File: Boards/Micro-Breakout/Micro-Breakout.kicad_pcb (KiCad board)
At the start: 2 copper layers, 92.7 x 54.6 mm, 38 parts, among them J1 Conn_01x04, J10 Conn_01x17, J11 Conn_01x04, J12 Conn_01x04, J13 Conn_01x02, J14 Conn_01x04, J16 Conn_01x04, J17 Conn_01x04, J18 Conn_01x04, J2 Conn_01x04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

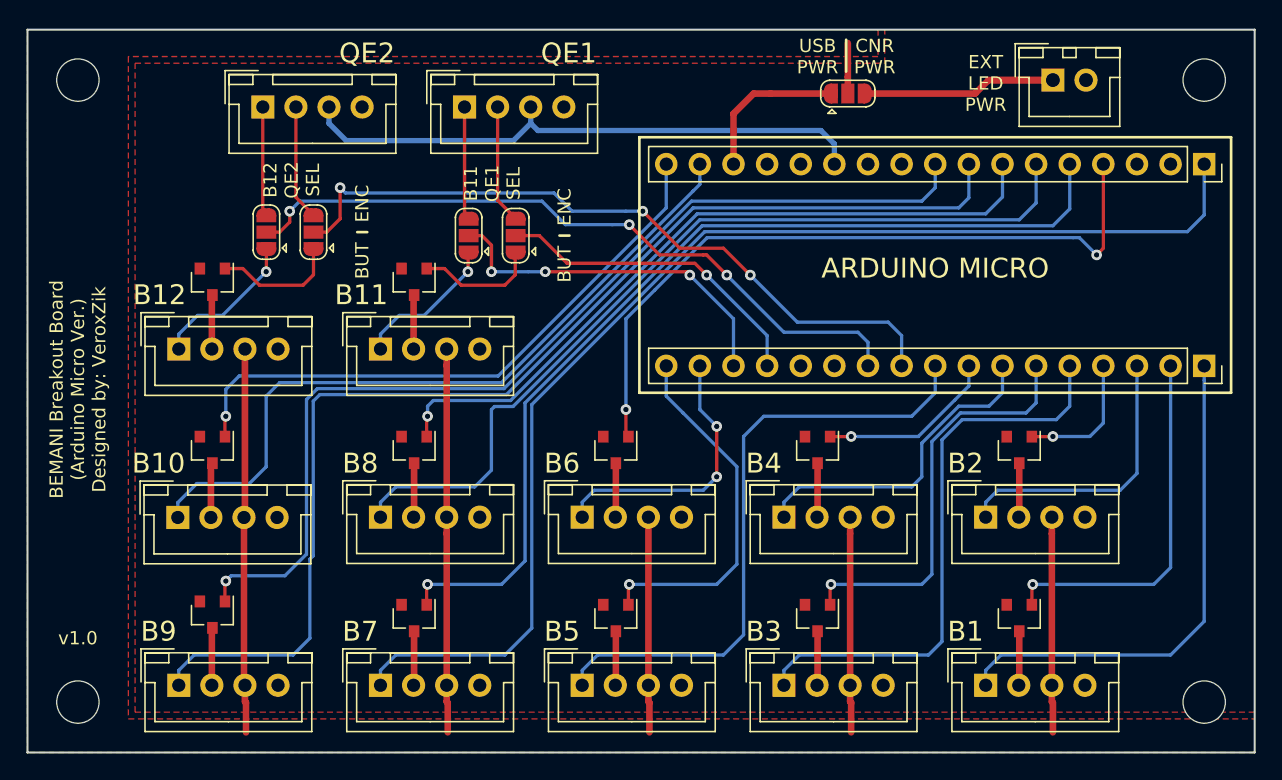
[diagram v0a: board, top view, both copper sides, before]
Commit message: Update both micro boards to v1.1
Fixes 5V on the LED connector
Adds pinout labels for Encoder / Button connectors
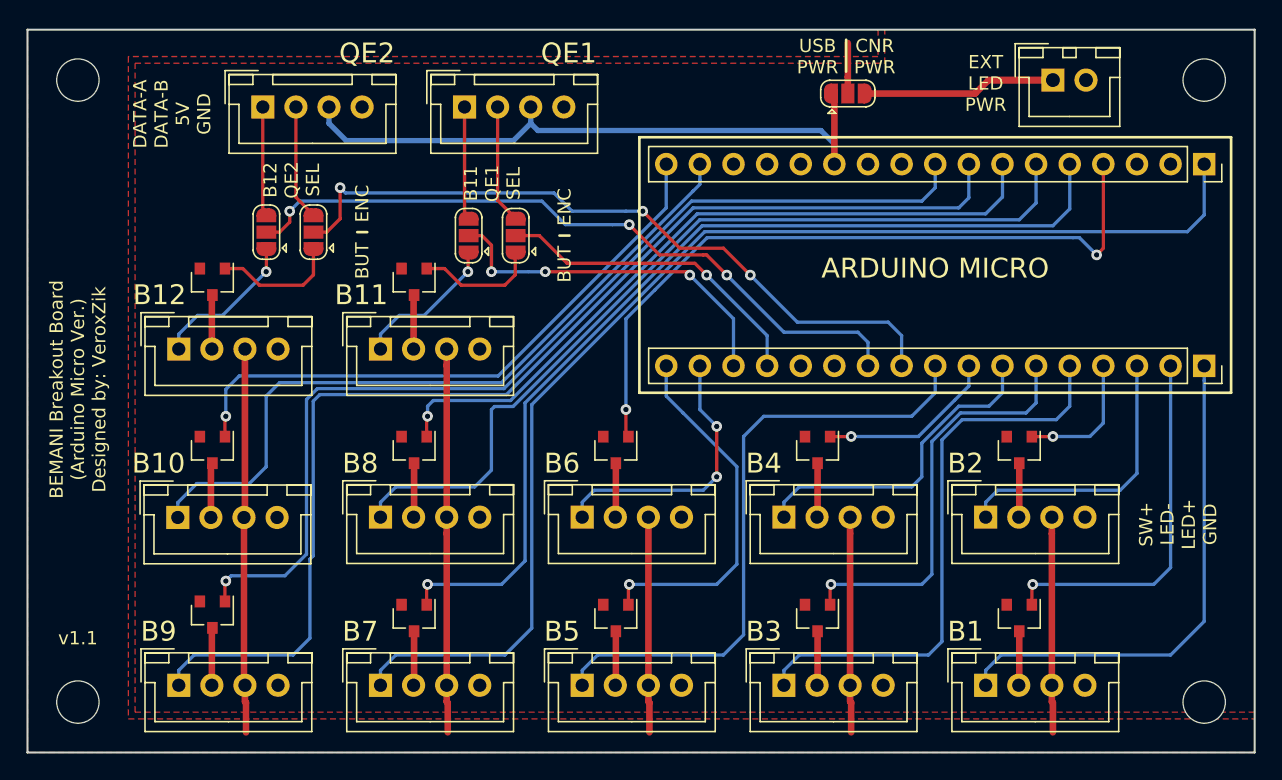
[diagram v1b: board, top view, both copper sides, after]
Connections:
- J7 pad 15: VBUS -> Net-(J7-Pad15)
- JP1 pad 1: VBUS -> +5V
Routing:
- net VBUS: track 11.8 -> 0.00 mm
- net +5V: track 43.9 -> 49.4 mm
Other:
- board text added: "DATA-A DATA-B 5V GND"
- board text added: "SW+ LED- LED+ GND"
- board text added: "v1.1"
- board text removed: "v1.0"

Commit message: Update Micro-Breakout board.
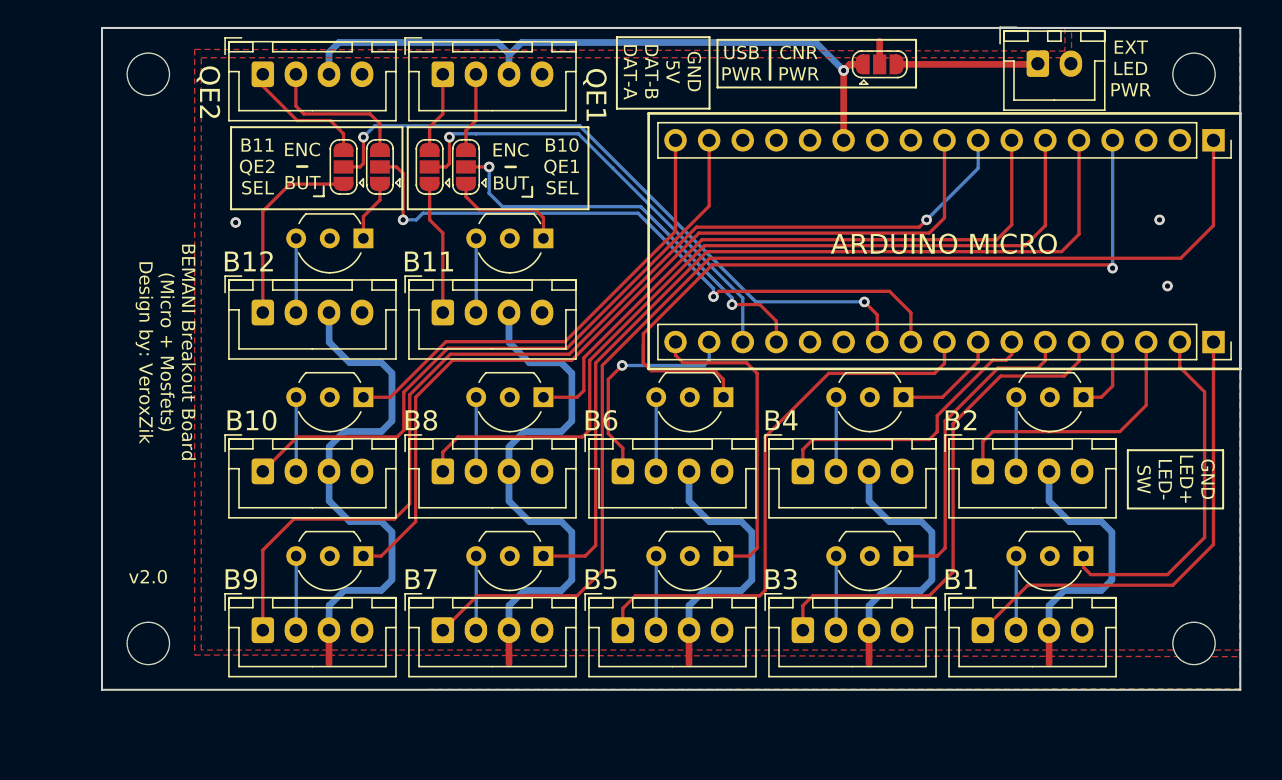
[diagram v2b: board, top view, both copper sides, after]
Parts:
- J1, J11, J12, J14, J16, J17, J18, J2, J3, J4, J5, J6, J8, J9: footprint Connectors_JST:JST_XH_B04B-XH-A_04x2.50mm_Straight -> Connector_JST:JST_XH_B4B-XH-A_1x04_P2.50mm_Vertical
- J13: footprint Connectors_JST:JST_XH_B02B-XH-A_02x2.50mm_Straight -> Connector_JST:JST_XH_B2B-XH-A_1x02_P2.50mm_Vertical
- Q1, Q10, Q11, Q12, Q2, Q3, Q4, Q5, Q6, Q7, Q8, Q9: value Si2302CDS -> 2N7000; footprint TO_SOT_Packages_SMD:SOT-23 -> Package_TO_SOT_THT:TO-92_Inline_Wide
- moved Q11 25.2 mm to (141.8, 103.4), turned to 180 degrees
- moved J17 20.1 mm to (134.2, 109.0)
- moved Q9 19.6 mm to (128.2, 103.4), turned to 180 degrees
- moved J14 16.8 mm to (120.7, 109.0)
- moved J12 12.8 mm to (120.7, 121.0)
- moved Q12 12.2 mm to (128.2, 127.4), turned to 180 degrees
- moved Q7 10.8 mm to (141.8, 127.4), turned to 180 degrees
- moved Q10 10.5 mm to (141.8, 115.4), turned to 180 degrees
- moved Q8 9.52 mm to (128.2, 115.4), turned to 180 degrees
- moved Q5 9.38 mm to (155.4, 127.4), turned to 180 degrees
- moved Q6 9.05 mm to (155.4, 115.4), turned to 180 degrees
- moved Q3 8.00 mm to (169.1, 127.4), turned to 180 degrees
- moved JP4 7.63 mm to (126.8, 98.0)
- moved Q4 7.61 mm to (169.1, 115.4), turned to 180 degrees
- moved J18 7.59 mm to (120.7, 133.0)
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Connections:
- J10 pad 13: Net-(J10-Pad13) -> unconnected-(J10-Pad13)
- J12 pad 1: /B11 -> /B10
- J14 pad 1: /B10 -> /B12
- J17 pad 1: /B12 -> /B11
- J7 pad 10: Net-(J7-Pad10) -> unconnected-(J7-Pad10)
- J7 pad 11: Net-(J7-Pad11) -> unconnected-(J7-Pad11)
- J7 pad 13: Net-(J7-Pad13) -> unconnected-(J7-Pad13)
- J7 pad 15: Net-(J7-Pad15) -> unconnected-(J7-Pad15)
- J7 pad 3: Net-(J7-Pad3) -> unconnected-(J7-Pad3)
- Q11 pad 1: /B12LED -> /B11LED
- Q8 pad 1: /B11LED -> /B10LED
- Q9 pad 1: /B10LED -> /B12LED
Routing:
- net /LED+: track 110.9 -> 147.7 mm
- net /B9LED: track 76.1 -> 65.8 mm, vias 1 -> 0
- net /B10LED: track 45.9 -> 35.6 mm, vias 1 -> 0
- net /B9: track 88.5 -> 79.0 mm, vias 0 -> 1
- net +12V: track 19.2 -> 10.7 mm
- net /B3LED: track 31.4 -> 23.9 mm, vias 1 -> 0
- net /PIN1: track 27.3 -> 34.3 mm, vias 3 -> 1
- net /PIN0: track 24.4 -> 31.3 mm, vias 1 -> 2
- net /B10: track 55.2 -> 48.7 mm
- net /B7LED: track 72.2 -> 65.7 mm, vias 1 -> 0
- net /B8LED: track 54.8 -> 48.6 mm, vias 1 -> 0
- net /B4LED: track 13.6 -> 8.23 mm, vias 1 -> 0
- net /B5: track 47.3 -> 42.0 mm
- net /B7: track 91.3 -> 86.4 mm
- net /B12LED: track 9.46 -> 4.62 mm
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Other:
- board size 92.7 x 54.6 mm -> 86 x 50 mm
- net class Default removed
- rule pad_to_mask_clearance: 0.2 -> 0
- board text added: "B10 QE1 SEL"
- board text added: "B11 QE2 SEL"
- board text added: "BEMANI Breakout Board (Micro + Mosfets) Design by: VeroxZik"
- board text added: "GND 5V DAT-B DAT-A"
- board text added: "GND LED+ LED- SW"
- board text added: "v2.0"
- board text removed: "B11 QE1 SEL"
- board text removed: "B12 QE2 SEL"
- board text removed: "BEMANI Breakout Board (Arduino Micro Ver.) Designed by: VeroxZik"
- board text removed: "DATA-A DATA-B 5V GND"
- board text removed: "SW+ LED- LED+ GND"
- board text removed: "v1.1"
